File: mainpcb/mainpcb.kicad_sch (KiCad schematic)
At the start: 16 parts, among them J1 Raspberry_Pi_2_3, J3 8P8C_Shielded, J4 Conn_01x03, J5 Conn_01x08, U1 PCA9615DP, U5 TCA9517ADGK

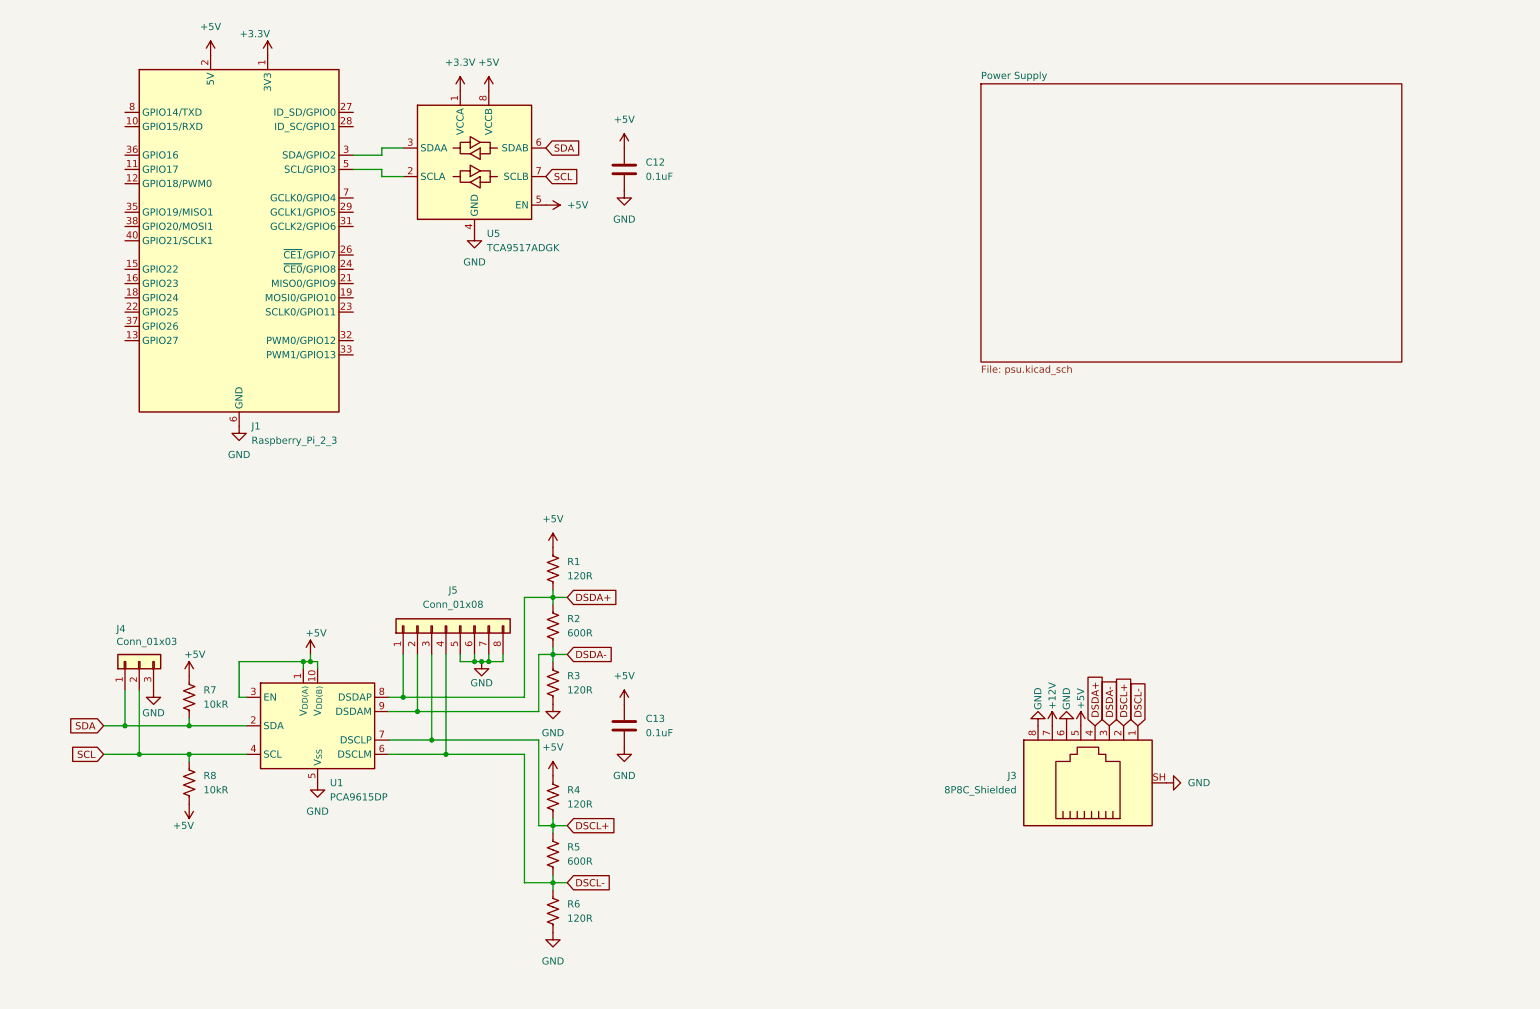
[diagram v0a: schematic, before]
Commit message: I2C transceivers, sheet hierarchy changes
Added I2C transceivers for both hands on the controller side, also changed sheet hierarchy to modularize controller board sheet somewhat
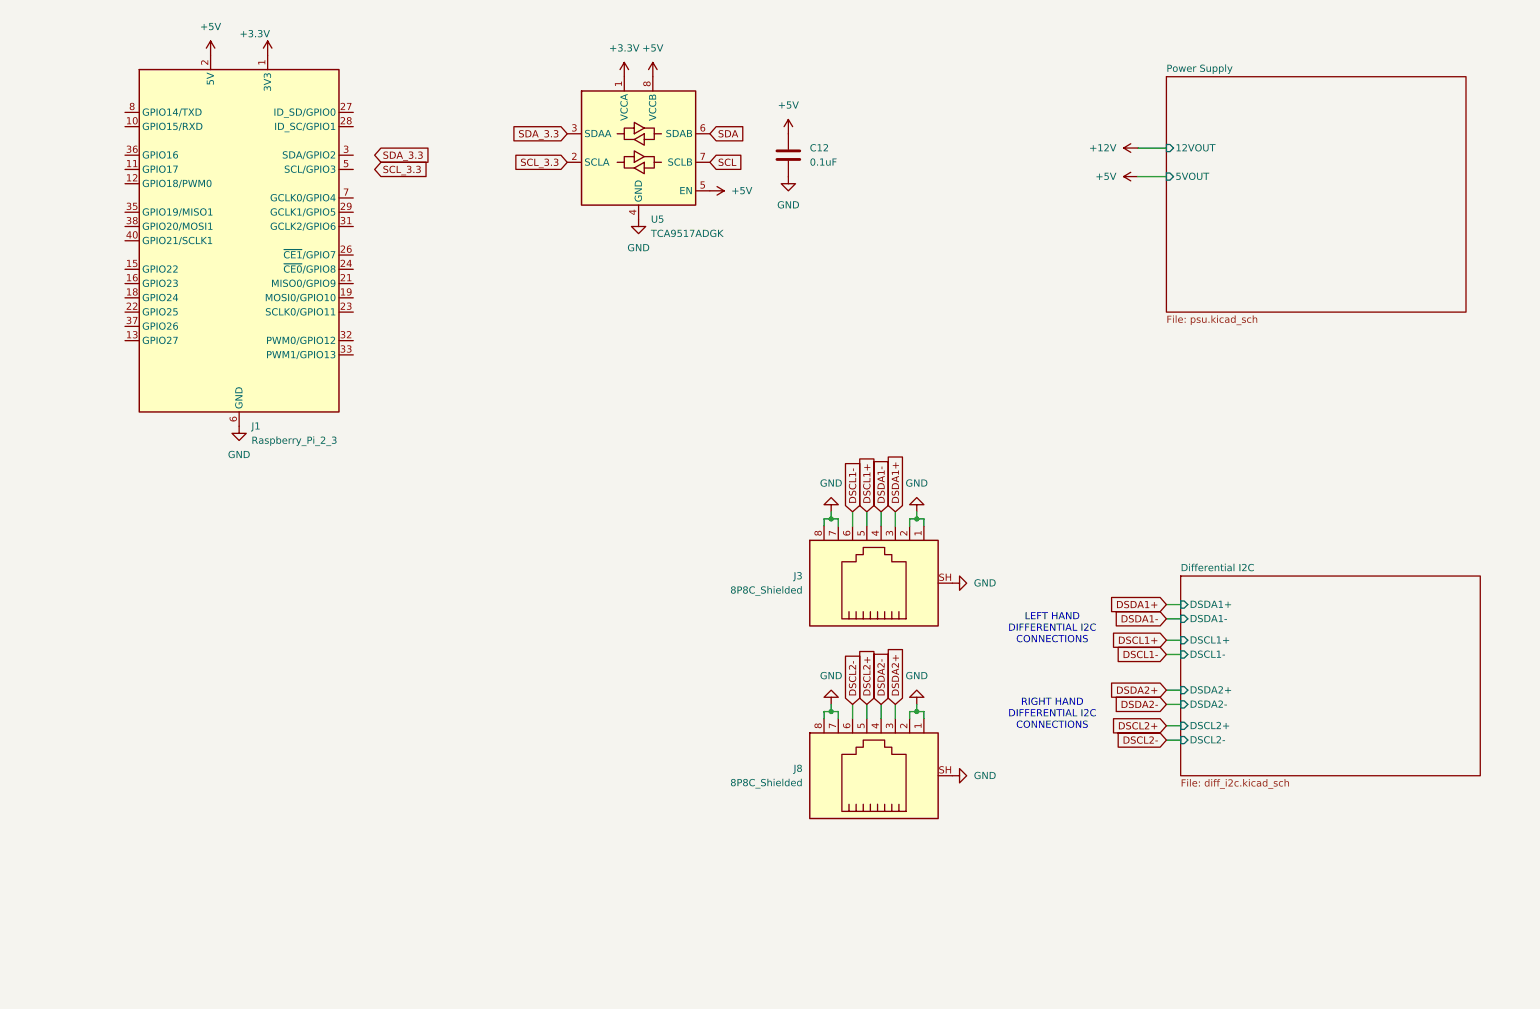
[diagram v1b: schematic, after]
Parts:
- removed C13: 0.1uF, Capacitor_THT:C_Disc_D8.0mm_W2.5mm_P5.00mm, symbol Device:C
- removed J4: Conn_01x03, Connector_PinHeader_2.54mm:PinHeader_1x03_P2.54mm_Vertical, symbol Connector_Generic:Conn_01x03
- removed J5: Conn_01x08, Connector_PinHeader_2.54mm:PinHeader_1x08_P2.54mm_Vertical, symbol Connector_Generic:Conn_01x08
- removed R1, R3, R4, R6: 120R, symbol Device:R_US
- removed R2, R5: 600R, symbol Device:R_US
- removed R7, R8: 10kR, symbol Device:R_US
- removed U1: PCA9615DP, Package_SO:TSSOP-10_3x3mm_P0.5mm, symbol Interface:PCA9615DP
- added J8: 8P8C_Shielded, Connector_RJ:RJ45_Amphenol_RJHSE5380, symbol Connector:8P8C_Shielded
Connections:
- net DSCL+ is gone; now on net GND: J3.2
- net DSCL- is gone; now on net GND: J3.1
- net +12V: no longer J3.7
- net +5V: no longer J3.5
- net GND: now also J3.7, J8.1, J8.2, J8.7, J8.8, J8.SH; no longer J3.6
- net at J1.5 (SCL/GPIO3): no longer U5.2 (SCLA)
- net at J1.3 (SDA/GPIO2): no longer U5.3 (SDAA)
- net DSDA+ renamed DSDA1-
- net DSDA- renamed DSDA1+
- new net DSCL1+: J3.5
- new net DSCL1-: J3.6
- new net DSCL2+: J8.5
- new net DSCL2-: J8.6
- new net DSDA2+: J8.3
- new net DSDA2-: J8.4
- new net SCL_3.3: U5.2 (SCLA)
- new net SDA_3.3: U5.3 (SDAA)
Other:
- added sheet Differential I2C (diff_i2c.kicad_sch)
- sheet Power Supply ports: added 12VOUT, 5VOUT; removed none
- note added: "LEFT HAND DIFFERENTIAL I2C CONNECTIONS"
- note added: "RIGHT HAND DIFFERENTIAL I2C CONNECTIONS"
- moved on the sheet: C12, J3, U5

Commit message: Added GPIO level shifter
Added general purpose TXB0108 level shifter to translate from 3.3V to 5V logic between the RPi and motor driver

Future connections will be for limit switches etc.
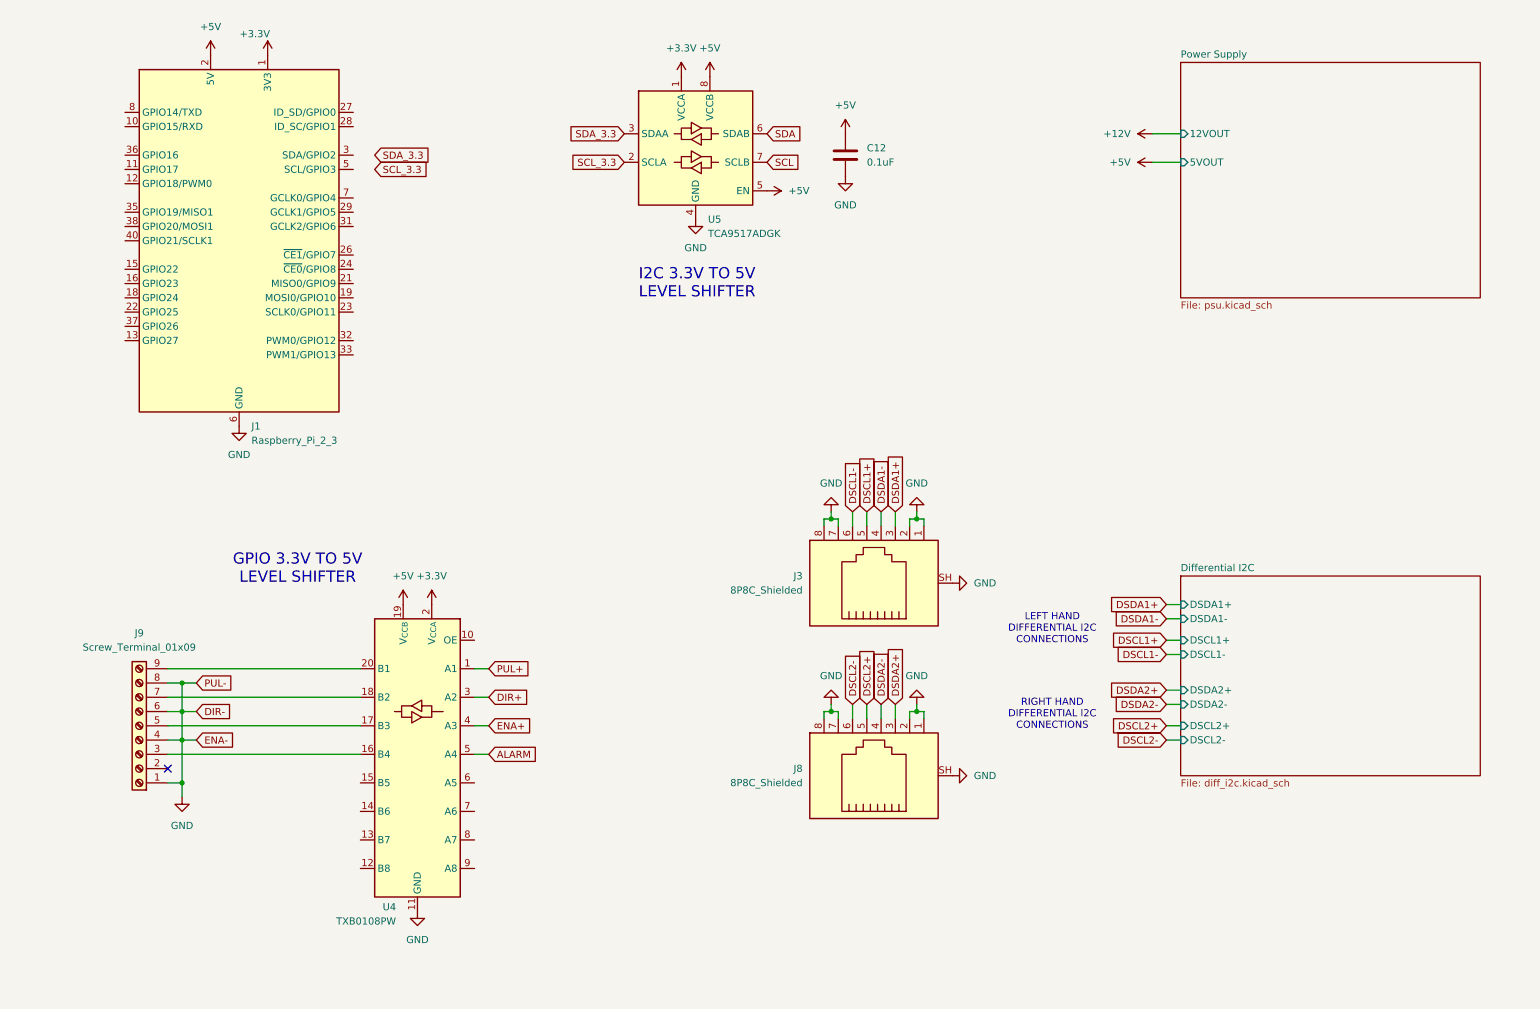
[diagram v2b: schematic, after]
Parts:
- added J9: Screw_Terminal_01x09, symbol Connector:Screw_Terminal_01x09
- added U4: TXB0108PW, Package_SO:TSSOP-20_4.4x6.5mm_P0.65mm, symbol Logic_LevelTranslator:TXB0108PW
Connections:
- net +3.3V: now also U4.2 (V_{CCA})
- net +5V: now also U4.19 (V_{CCB})
- net GND: now also J9.1 (Pin_1), J9.4 (Pin_4), J9.6 (Pin_6), J9.8 (Pin_8), U4.11 (GND)
- new net: J9.3 (Pin_3), U4.16 (B4)
- new net: J9.5 (Pin_5), U4.17 (B3)
- new net: J9.7 (Pin_7), U4.18 (B2)
- new net: J9.9 (Pin_9), U4.20 (B1)
- new net ALARM: U4.5 (A4)
- new net DIR+: U4.3 (A2)
- new net ENA+: U4.4 (A3)
- new net PUL+: U4.1 (A1)
- no-connect marks 0 -> 1
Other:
- note added: "GPIO 3.3V TO 5V LEVEL SHIFTER"
- note added: "I2C 3.3V TO 5V LEVEL SHIFTER"
- moved on the sheet: C12, U5

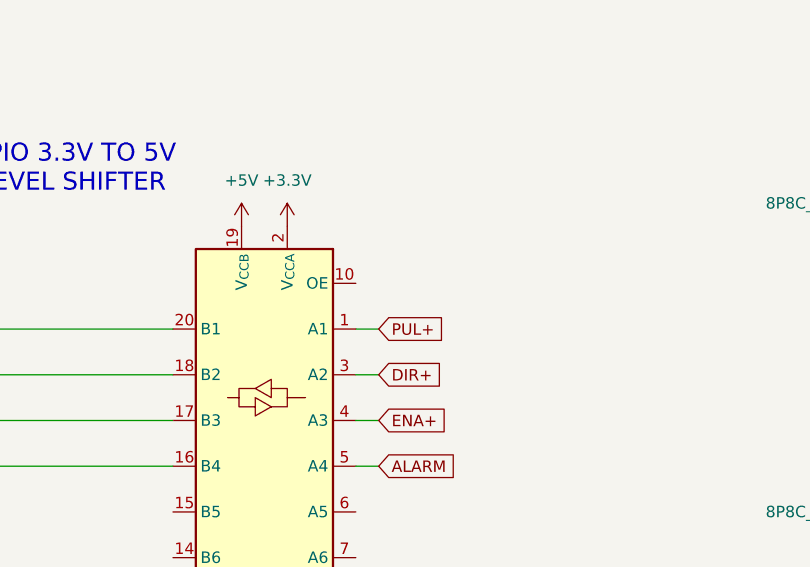
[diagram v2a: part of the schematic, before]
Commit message: Tie output enable pin on TXB0108 to 3.3V
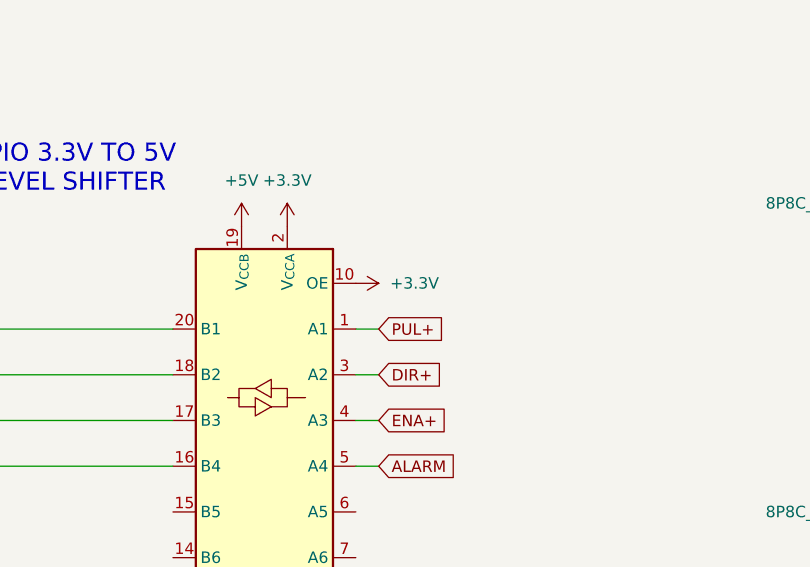
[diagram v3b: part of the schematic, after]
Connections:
- net +3.3V: now also U4.10 (OE)
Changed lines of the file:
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@@
+	)
+	(symbol
+		(lib_id "power:+3.3V")
+		(at 95.25 128.27 270)
+		(unit 1)
+		(exclude_from_sim no)
+		(in_bom yes)
+		(on_board yes)
+		(dnp no)
+		(fields_autoplaced yes)
+		(property "Reference" "#PWR020"
+			(at 91.44 128.27 0)
+			(effects
+				(font
+					(size 1.27 1.27)
+				)
+				(hide yes)
+			)
+		)
+		(property "Value" "+3.3V"
+			(at 99.06 128.2699 90)
+			(effects
+				(font
+					(size 1.27 1.27)
+				)
+				(justify left)
+			)
+		)
+		(property "Footprint" ""
+			(at 95.25 128.27 0)
+			(effects
+				(font
+					(size 1.27 1.27)
+				)
+				(hide yes)
+			)
+		)
+		(property "Datasheet" ""
+			(at 95.25 128.27 0)
+			(effects
+				(font
+					(size 1.27 1.27)
+				)
+				(hide yes)
+			)
+		)
+		(property "Description" "Power symbol creates a global label with name \"+3.3V\""
+			(at 95.25 128.27 0)
+			(effects
+				(font
+					(size 1.27 1.27)
+				)
+				(hide yes)
+			)
+		)
+		(pin "1"
+		)
+		(instances
+			(project "mainpcb"
+				(path "/8e899647-a0f4-47d2-9d4a-2e9de2221eca"
+					(reference "#PWR020")
+					(unit 1)
+				)
+			)
+		)
 	)
 	(symbol

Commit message: Major update
Hand PCB mostly complete
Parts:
- added J10, J11: Conn_02x02_Top_Bottom, Connector_Molex:Molex_Mini-Fit_Jr_5569-04A2_2x02_P4.20mm_Horizontal, symbol Connector_Generic:Conn_02x02_Top_Bottom
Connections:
- net +12V: now also J10.4 (Pin_4), J11.4 (Pin_4)
- net +5V: now also J10.3 (Pin_3), J11.3 (Pin_3)
- net GND: now also J10.1 (Pin_1), J10.2 (Pin_2), J11.1 (Pin_1), J11.2 (Pin_2)
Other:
- moved on the sheet: C12, J3, J8, J9, U4, U5
